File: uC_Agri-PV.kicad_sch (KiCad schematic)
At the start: 0 parts

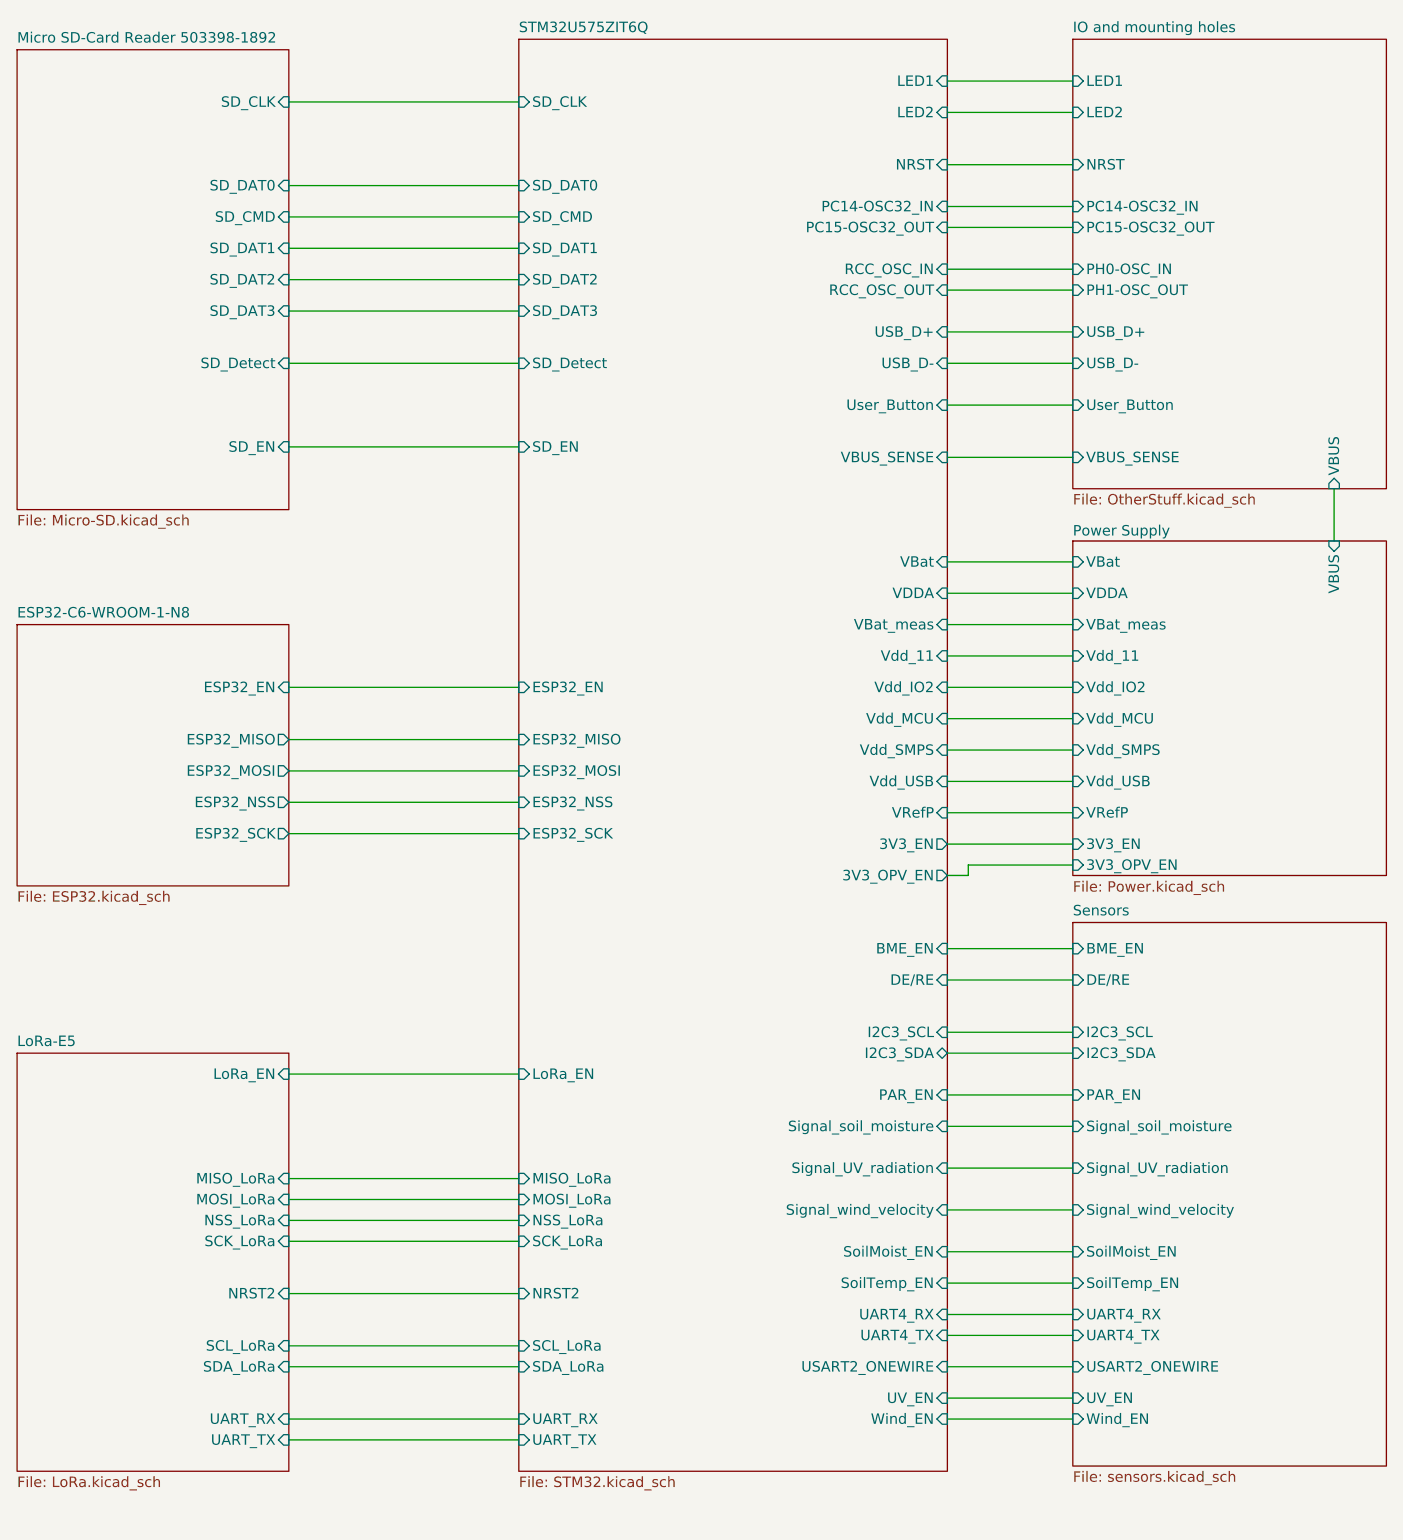
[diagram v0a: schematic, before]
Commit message: Add SamacSys & CAPPRD library; update KiCad
Add a new SamacSys parts library and a complete CAPPRD500 footprint/package set (870585375004) with multi-EDA exports and 3D STEP models. Also add sym-lib-table and SamacSys parts entries, and update KiCad project files (schematics, PCB, project file and generated PDFs) to reference the new parts and footprints.
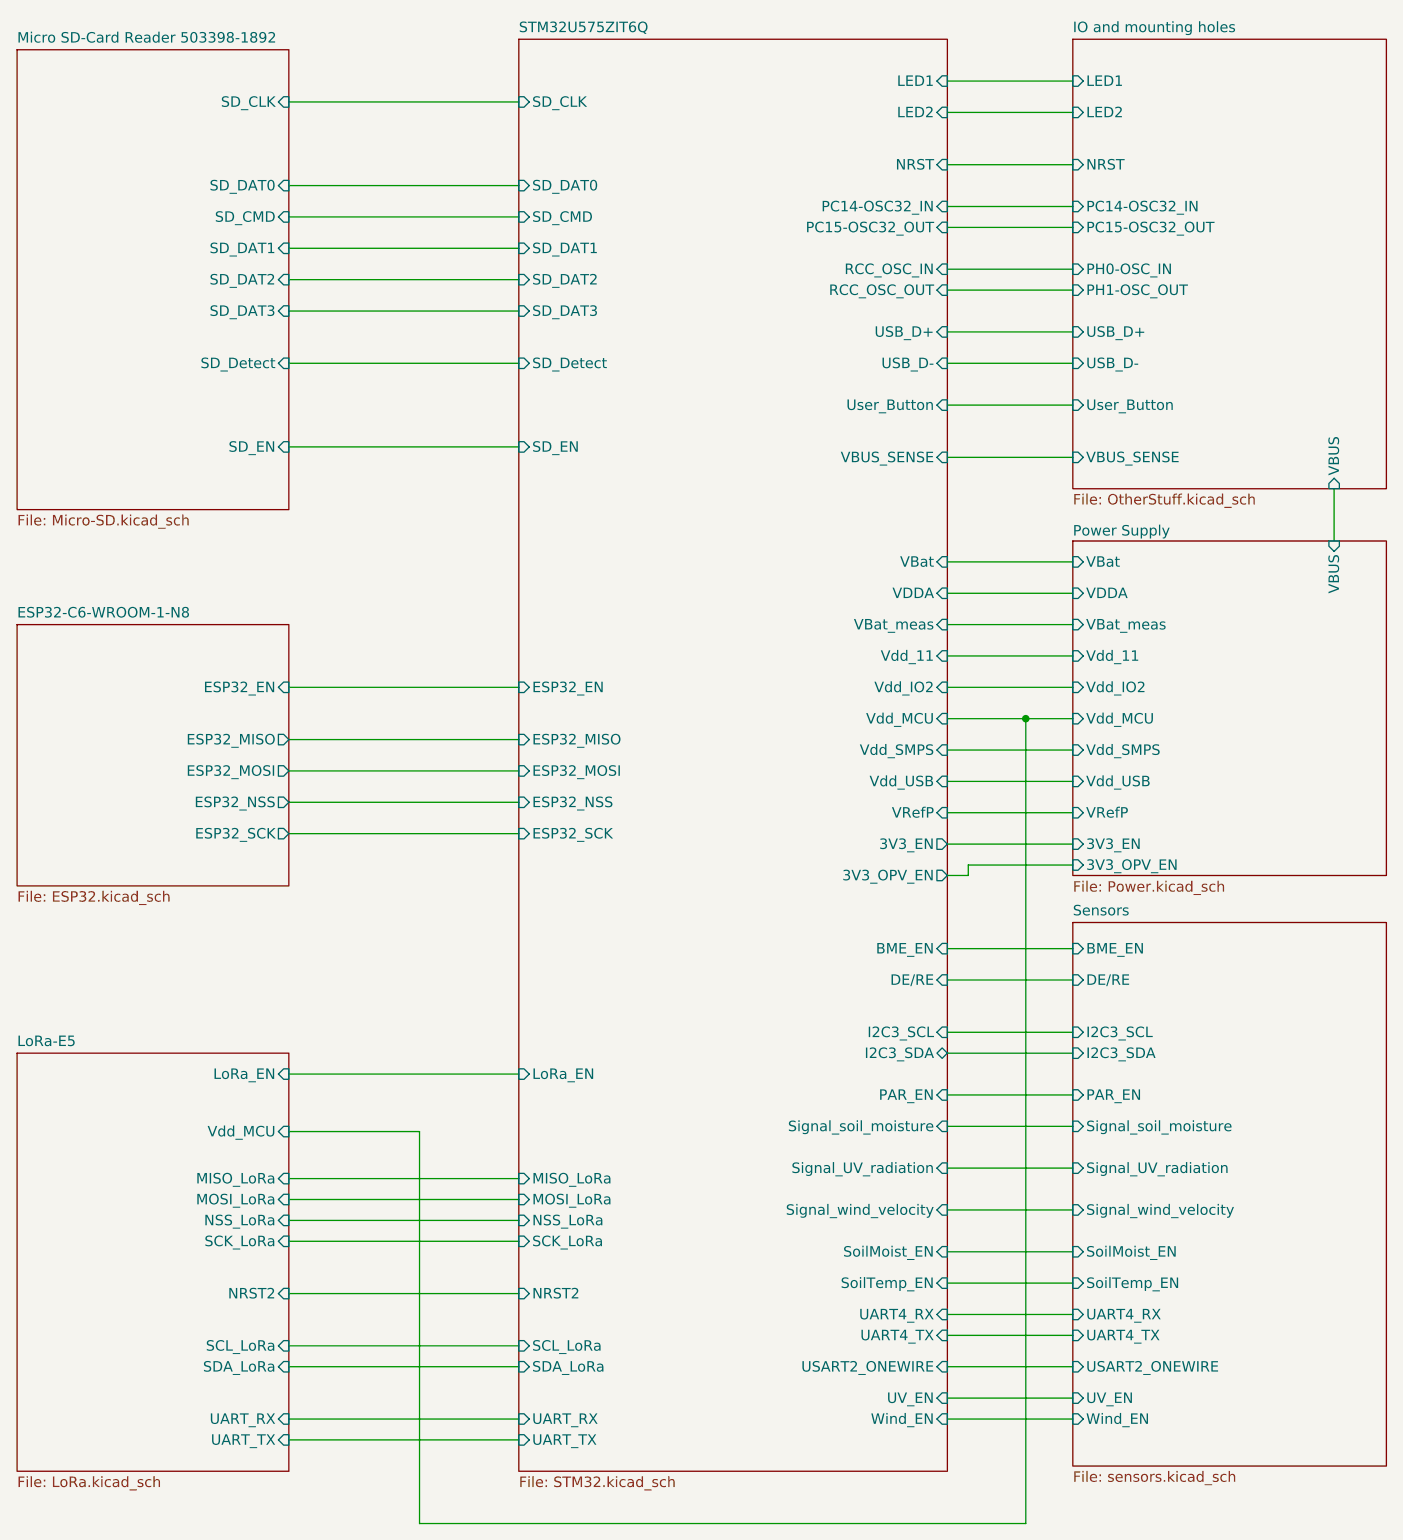
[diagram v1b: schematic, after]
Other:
- sheet LoRa-E5 ports: added Vdd_MCU; removed none
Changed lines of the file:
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@@
 		(company "Hochschule Karlsruhe ")
 	)
+	(junction
+		(at 141.605 130.81)
+		(diameter 0)
+		(color 0 0 0 0)
+	)
 	(wire
 		(pts
@@
 	(wire
 		(pts
+			(xy 52.07 180.975) (xy 67.945 180.975)
+		)
+		(stroke
+			(width 0)
+			(type default)
+		)
+	)
+	(wire
+		(pts
 			(xy 132.08 195.58) (xy 147.32 195.58)
 		)
@@
 	(wire
 		(pts
+			(xy 67.945 228.6) (xy 141.605 228.6)
+		)
+		(stroke
+			(width 0)
+			(type default)
+		)
+	)
+	(wire
+		(pts
 			(xy 132.08 76.2) (xy 147.32 76.2)
 		)
@@
 	(wire
 		(pts
+			(xy 67.945 180.975) (xy 67.945 228.6)
+		)
+		(stroke
+			(width 0)
+			(type default)
+		)
+	)
+	(wire
+		(pts
 			(xy 132.08 53.34) (xy 147.32 53.34)
 		)
@@
 	(wire
 		(pts
+			(xy 141.605 228.6) (xy 141.605 130.81)
+		)
+		(stroke
+			(width 0)
+			(type default)
+		)
+	)
+	(wire
+		(pts
 			(xy 132.08 119.38) (xy 147.32 119.38)
 		)
@@
 	(wire
 		(pts
-			(xy 132.08 130.81) (xy 147.32 130.81)
+			(xy 132.08 130.81) (xy 141.605 130.81)
 		)
 		(stroke
@@
 		(pts
 			(xy 52.07 97.79) (xy 80.01 97.79)
+		)
+		(stroke
+			(width 0)
+			(type default)
+		)
+	)
+	(wire
+		(pts
+			(xy 141.605 130.81) (xy 147.32 130.81)
 		)
 		(stroke
@@
 			(effects
 				(font
+					(size 1.27 1.27)
+				)
+				(justify right)
+			)
+		)
+		(pin "Vdd_MCU" input
+			(at 52.07 180.975 0)
+			(effects
+				(font
